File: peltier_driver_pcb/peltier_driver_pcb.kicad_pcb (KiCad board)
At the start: 2 copper layers, 47 x 34 mm, 29 parts, among them J1 Peltier V-, J10 GA10K4A1_NTC, J2 Driver V-, J21 Peltier V-, J22 Driver V-, J25 Peltier V+, J28 Driver V+, J3 GA10K4A1_NTC, J4 Peltier V+, J5 Driver V+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

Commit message: v1 PCB ready for show
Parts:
- added D1: LED, LED_THT:LED_D3.0mm, F.Cu at (158.5, 58.0)
- added J6: Conn_02x10_Top_Bottom, Connector_PinHeader_2.54mm:PinHeader_2x10_P2.54mm_Vertical, F.Cu at (162.5, 58.6)
- added R10: 180, Resistor_THT:R_Axial_DIN0204_L3.6mm_D1.6mm_P2.54mm_Vertical, F.Cu at (156.0, 61.3)
- moved J9 2.26 mm to (110.0, 58.6)
- moved J10 2.13 mm to (151.2, 55.2)
- moved J3 1.21 mm to (151.2, 84.7)
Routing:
- net +5V: track 58.6 -> 70.4 mm
- net GND: track 16.7 -> 8.72 mm, vias 4 -> 2
- net +3V3: track 16.4 -> 20.5 mm
- net Net-(D1-Pad1): track 0.00 -> 3.35 mm
- net T_sense1: track 34.5 -> 36.9 mm
- net I_sense_1: track 16.5 -> 18.7 mm
- net I_sense_2: track 24.3 -> 26.4 mm
- net T_sense2: track 42.9 -> 44.9 mm
- net Net-(J10-Pad2): track 19.0 -> 21.0 mm
- net SCL: track 6.02 -> 7.99 mm
- net SDA: track 5.95 -> 7.69 mm
- net Net-(J3-Pad2): track 17.2 -> 18.0 mm
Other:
- board size 47 x 34 mm -> 61 x 33 mm
- board text added: "3V3"
- board text added: "5V"
- board text added: "A0"
- board text added: "A1"
- board text added: "A2"
- board text added: "A3"
- board text added: "A4"
- board text added: "D0"
- board text added: "D1"
- board text added: "D2"
- board text added: "D3"
- board text added: "GND"
- board text added: "I_2"
- board text added: "PWM0"
- board text added: "PWM1"
- board text added: "PWR"
- board text added: "SCL"
- board text added: "SDA"
- board text added: "T_1"
- board text added: "T_2"

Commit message: updating gerber files for UI PCB
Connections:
- J9 pad 1: D0 -> A0
- J9 pad 11: A1 -> D0
- J9 pad 13: A2 -> D1
- J9 pad 15: A3 -> D2
- J9 pad 16: A4 -> D3
- J9 pad 3: D1 -> A1
- J9 pad 5: D2 -> A2
- J9 pad 7: D3 -> A3
- J9 pad 9: A0 -> A4
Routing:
- net GND: track 8.72 -> 15.2 mm, vias 2 -> 3
- net Net-(J3-Pad2): track 18.0 -> 21.3 mm, vias 0 -> 1
- net Net-(J10-Pad2): track 21.0 -> 21.3 mm, vias 0 -> 1

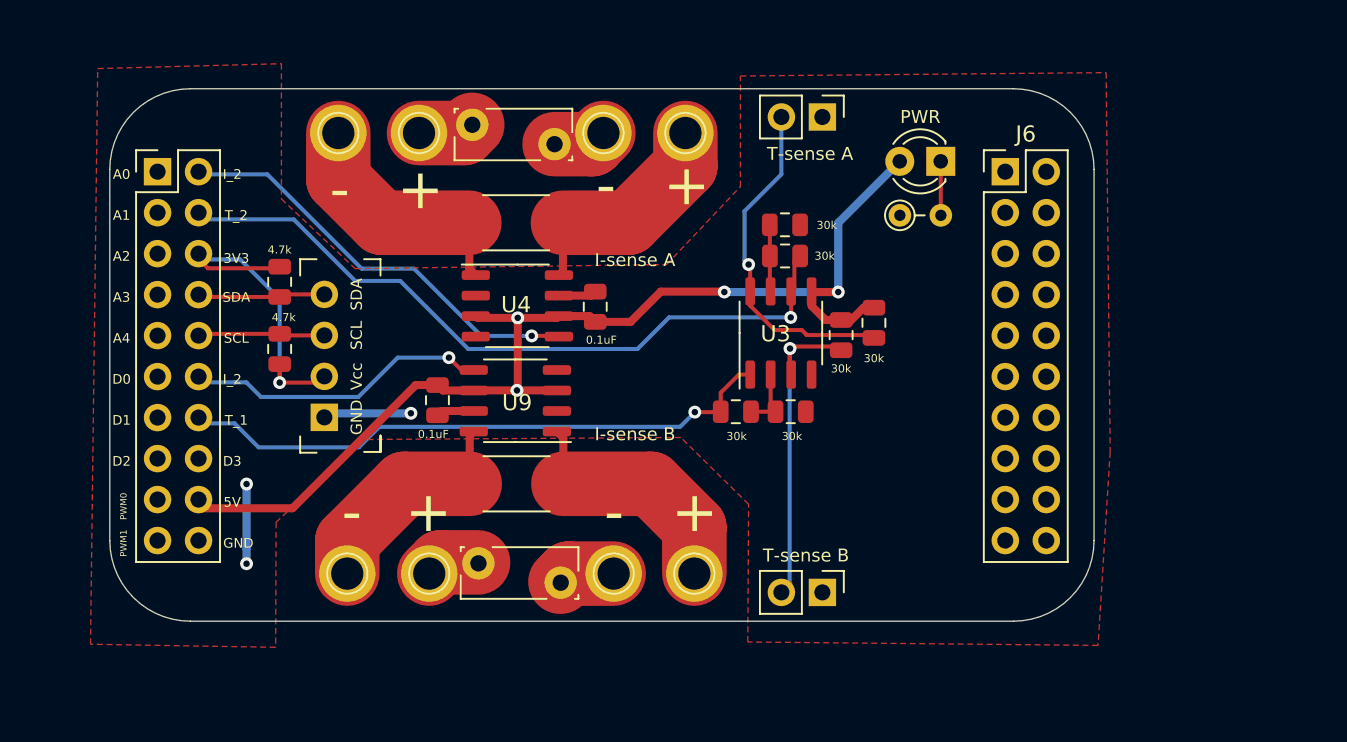
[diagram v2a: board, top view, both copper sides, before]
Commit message: better arduino ftprnt lib, first iteration of shield PCBs
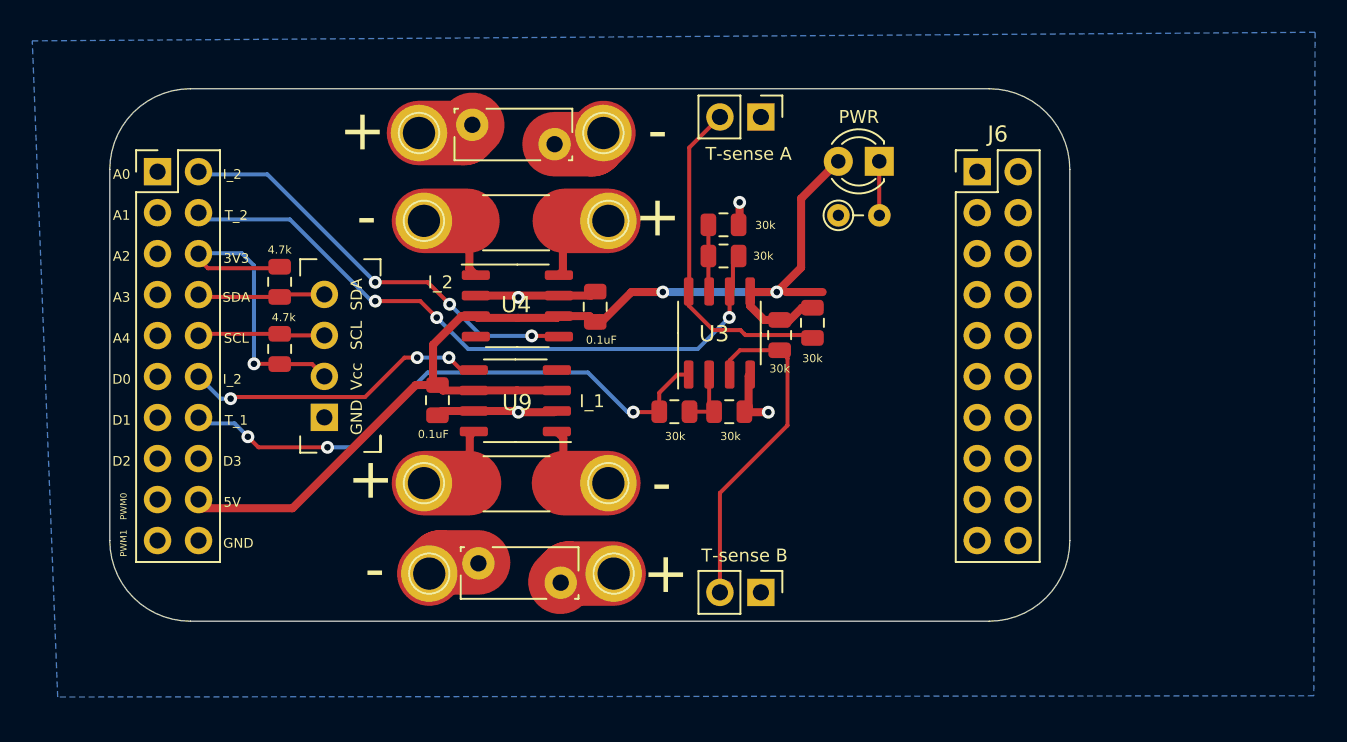
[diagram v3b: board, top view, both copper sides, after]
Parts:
- moved J25 7.73 mm to (137.9, 77.9)
- moved J4 7.60 mm to (126.5, 61.7)
- moved J28 7.35 mm to (126.5, 77.9)
- moved J5 7.24 mm to (137.9, 61.7)
- moved D1 3.81 mm to (154.7, 58.0)
- moved R10 3.81 mm to (152.2, 61.3)
- moved R3 3.81 mm to (148.5, 68.8)
- moved R4 3.81 mm to (142.0, 73.5)
- moved R5 3.81 mm to (145.4, 73.5)
- moved R7 3.81 mm to (145.0, 63.9)
- moved R8 3.81 mm to (145.0, 61.9)
- moved R9 3.81 mm to (150.5, 68.0)
- moved U3 3.81 mm to (144.8, 68.6)
- moved J10 3.81 mm to (147.4, 55.2)
- moved J3 3.81 mm to (147.4, 84.7)
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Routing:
- net Net-(J4-Pad1): track 15.5 -> 6.10 mm
- net Net-(J25-Pad1): track 15.5 -> 6.16 mm
- net Net-(J5-Pad1): track 14.4 -> 6.05 mm
- net Net-(J28-Pad1): track 14.4 -> 6.14 mm
- net GND: track 15.2 -> 20.9 mm, vias 3 -> 4
- net T_sense2: track 44.9 -> 41.1 mm, vias 1 -> 3
- net Net-(J3-Pad2): track 21.3 -> 23.2 mm, vias 1 -> 0
- net T_sense1: track 37.3 -> 35.5 mm, vias 1 -> 3
- net +5V: track 70.4 -> 70.7 mm, vias 4 -> 2
- net Net-(J10-Pad2): track 21.3 -> 21.0 mm, vias 1 -> 0
- net I_sense_1: track 18.7 -> 19.0 mm, vias 1 -> 3
- net I_sense_2: vias 1 -> 3
- added copper zone on B.Cu, net GND
- removed copper zone on F.Cu, net GND
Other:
- board size 61 x 33 mm -> 59.5 x 33 mm
- board text added: "I_1"
- board text removed: "I-sense A"
- board text removed: "I-sense B"

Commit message: matching PCB dimensions to each other
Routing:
- net +5V: track 70.7 -> 68.4 mm
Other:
- board size 59.5 x 33 mm -> 61.3 x 32.9 mm
- board text added: "D12"
- board text added: "D13"
- board text added: "D4"
- board text added: "D7"
- board text added: "D8"
- board text added: "PWM2"
- board text added: "PWM3"
- board text added: "PWM4"
- board text added: "PWM5"
- board text removed: "A2"
- board text removed: "A3"
- board text removed: "A4"
- board text removed: "D3"
- board text removed: "T-sense A"
- board text removed: "T-sense B"
